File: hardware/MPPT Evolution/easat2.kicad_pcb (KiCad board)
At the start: 2 copper layers, 97 parts, among them J1 Conn_01x10, P1 CONN_01X02, P2 CONN_01X02, P3 CONN_01X02, P4 CONN_01X02, P5 CONN_01X02, P6 CONN_01X02, U1 LTC3129, U2 LTC3129, U3 LTC3129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

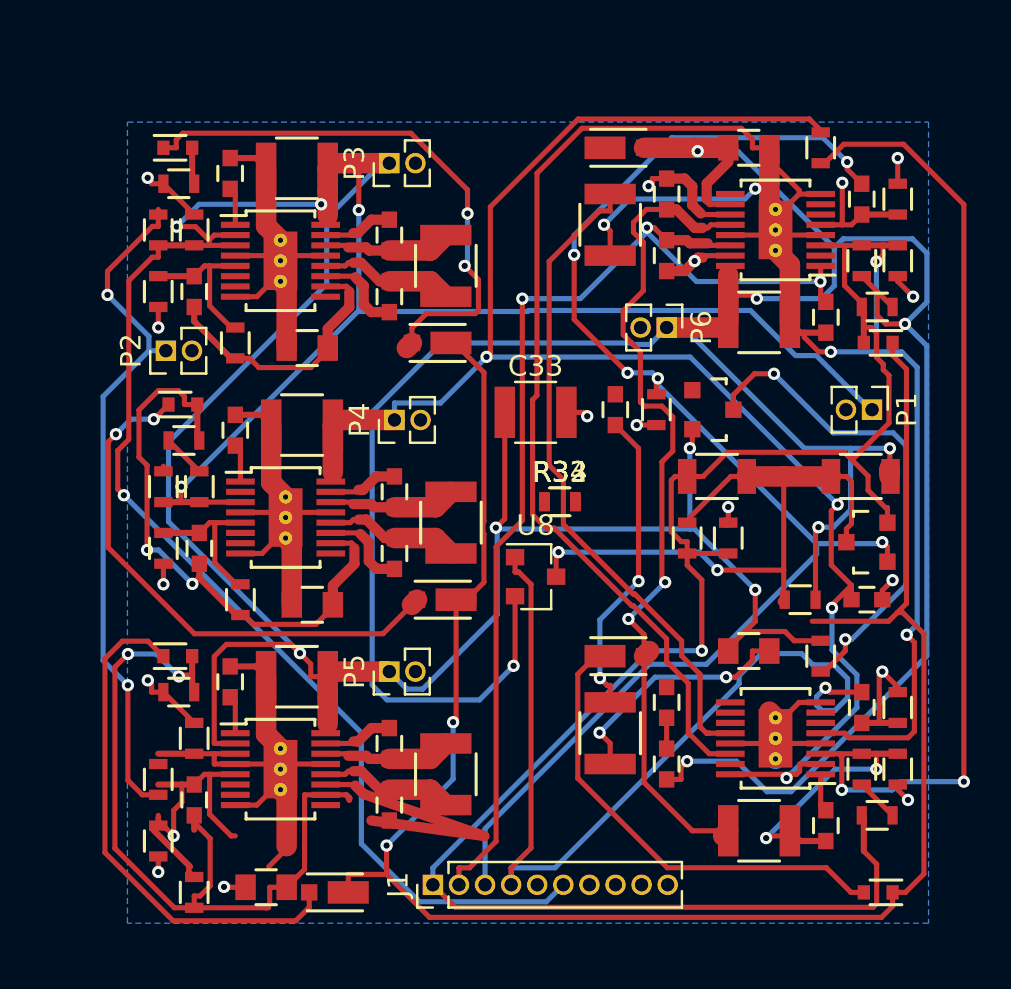
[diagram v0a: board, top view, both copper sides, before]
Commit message: MPPT board - Added holes, size set to 42mm, full routed
MPPT board - Added holes, size set to 42mm, full routed
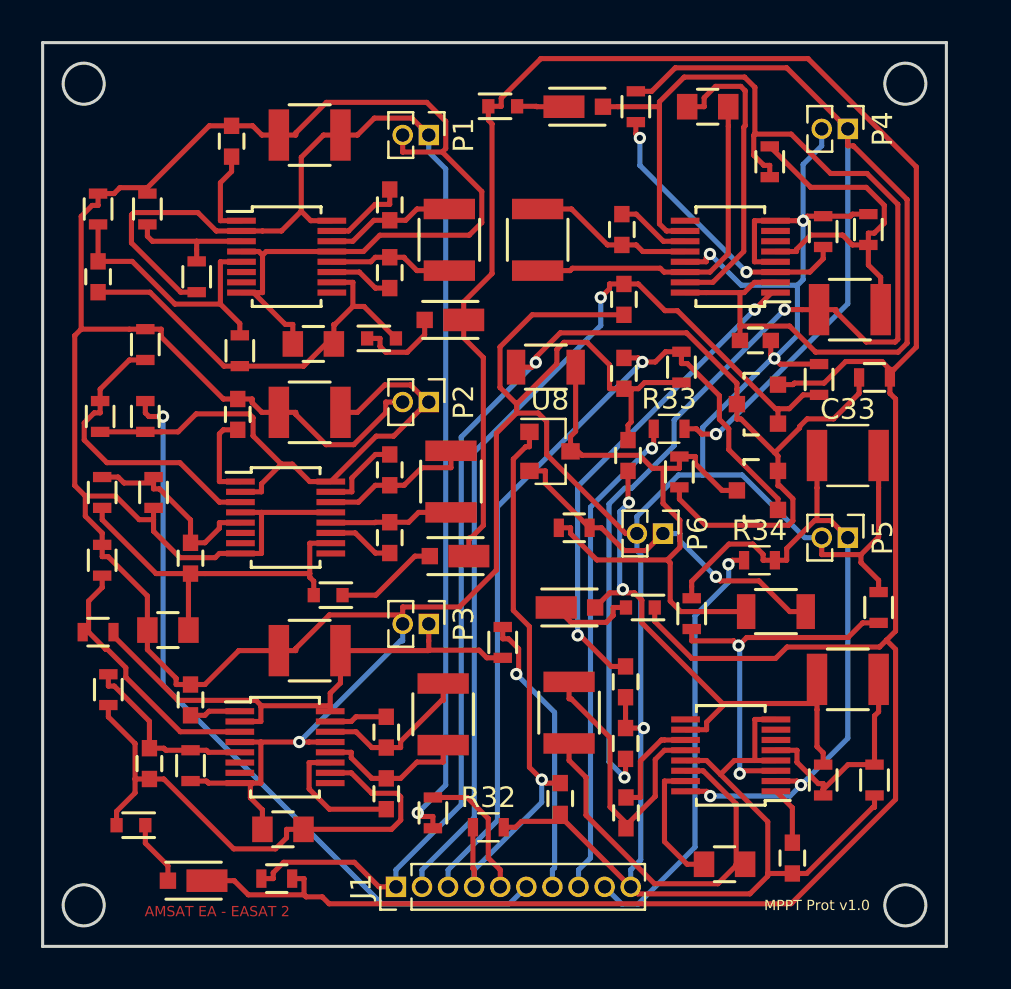
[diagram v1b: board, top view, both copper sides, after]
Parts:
- moved C26 30.7 mm to (150.1, 91.2)
- moved R1 30.7 mm to (140.9, 119.6)
- moved R21 29.4 mm to (133.3, 122.8)
- moved C25 26.4 mm to (158.4, 121.8)
- moved P4 26.2 mm to (161.1, 86.3), turned to 270 degrees
- moved R5 25.9 mm to (127.0, 90.2), turned to 90 degrees
- moved P1 25.4 mm to (140.7, 86.6)
- moved P5 23.3 mm to (161.1, 106.2), turned to 270 degrees
- moved P3 22.5 mm to (140.7, 110.4), turned to 270 degrees
- moved D7 21.6 mm to (144.3, 85.2), turned to 180 degrees
- moved C27 19.6 mm to (150.3, 119.6)
- moved D8 18.1 mm to (151.0, 109.6)
- moved R6 17.9 mm to (124.7, 100.3)
- moved R3 16.6 mm to (144.3, 111.3)
- moved R32 16.2 mm to (143.6, 120.3)
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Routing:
- net GND: track 114.2 -> 306.9 mm, vias 17 -> 5
- net Net-(C28-Pad1): track 69.9 -> 16.9 mm, vias 2 -> 0
- net Net-(P6-Pad1): track 66.9 -> 17.5 mm, vias 3 -> 1
- net Net-(D4-Pad1): track 92.0 -> 136.0 mm, vias 2 -> 0
- net Net-(R26-Pad2): track 46.6 -> 14.1 mm
- net I_BATT: track 67.9 -> 42.4 mm, vias 5 -> 1
- net PV3_IN: track 51.6 -> 26.4 mm, vias 1 -> 0
- net Net-(C19-Pad2): track 42.0 -> 17.7 mm, vias 3 -> 0
- net Net-(C26-Pad2): track 32.2 -> 8.04 mm
- net PV4_OUT: track 0.00 -> 23.9 mm, vias 0 -> 1
- net Net-(D1-Pad1): track 27.4 -> 4.39 mm, vias 2 -> 0
- net Net-(C24-Pad1): track 1.50 -> 23.7 mm, vias 0 -> 2
- net Net-(D3-Pad1): track 25.3 -> 3.16 mm
- net Net-(D2-Pad1): track 26.3 -> 5.04 mm, vias 2 -> 0
- net PV5_OUT: track 0.00 -> 21.2 mm, vias 0 -> 1
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- removed copper zone on B.Cu, net GND
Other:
- board outline added: 44 x 44 mm
- board text added: "AMSAT EA - EASAT 2"
- board text added: "MPPT Prot v1.0"

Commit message: Added ground planes to MPPT evolution
Added ground planes to MPPT evolution. Deleted big PCB version
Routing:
- added copper zone on B.Cu, net GND
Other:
- board text removed: "AMSAT-EA"
- board text removed: "EA4GPZ EA4GQS EA4GVA"
- board text removed: "EASAT-2"
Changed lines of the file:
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@@
   (general
     (links 197)
-    (no_connects 197)
+    (no_connects 0)
     (area 121.794999 82.054999 165.945001 126.205001)
     (thickness 1.6)
-    (drawings 19)
+    (drawings 16)
     (tracks 958)
     (zones 0)
@@
     (aux_axis_origin 174.06734 114.41544)
     (grid_origin 164.87 86.13)
-    (visible_elements 7FFEF7FF)
+    (visible_elements 7FFEFFFF)
     (pcbplotparams
-      (layerselection 0x002a0_80000001)
+      (layerselection 0x012a0_80000001)
       (usegerberextensions false)
       (excludeedgelayer true)
@@
       (drillshape 0)
       (scaleselection 1)
-      (outputdirectory "Gerber Files/"))
+      (outputdirectory ""))
   )
   (net 0 "")
@@
     (effects (font (size 0.5 0.5) (thickness 0.125)))
   )
-  (gr_text AMSAT-EA (at 138.75 123) (layer B.SilkS)
-    (effects (font (size 2 2) (thickness 0.3)) (justify mirror))
-  )
-  (gr_text "EA4GPZ\nEA4GQS\nEA4GVA" (at 149.75 114) (layer B.SilkS)
-    (effects (font (size 1.5 1.5) (thickness 0.3)) (justify mirror))
-  )
-  (gr_text EASAT-2 (at 156.5 87.75) (layer B.SilkS)
-    (effects (font (size 2 2) (thickness 0.5)) (justify mirror))
-  )
   (via (at 140.1342 119.63) (size 0.6) (layers F.Cu B.Cu) (net 1))
   (segment (start 136.37 86.63) (end 135.5447 86.63) (width 0.25) (layer F.Cu) (net 1))
@@
   (segment (start 153.17 118.08) (end 152.1447 118.08) (width 0.25) (layer F.Cu) (net 63))
   (segment (start 154.07 122.13) (end 153.2447 122.13) (width 0.25) (layer F.Cu) (net 63))
+  (zone (net 2) (net_name GND) (layer B.Cu) (hatch edge 0.508)
+    (connect_pads (clearance 0.508))
+    (min_thickness 0.254)
+    (fill yes (arc_segments 16) (thermal_gap 0.508) (thermal_bridge_width 0.508))
+    (polygon
+      (pts
+        (xy 123.07 83.13) (xy 164.77 83.13) (xy 164.87 125.03) (xy 122.87 125.13)
+      )
+    )
+  )
 )
